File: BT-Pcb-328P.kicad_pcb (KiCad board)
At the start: 2 copper layers, 57 x 57 mm, 61 parts, among them J1 USB_B_Micro, J2 FTDI, J3 ICSP, J4 ANT, J5 Si7021, J6 Vin, P1 MYSX_2.6, Q1 FDN338P, Q2 FDN337N, Q3 FDN337N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

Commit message: Development 3
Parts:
- added C13: 100uF, Capacitor_SMD:CP_Elec_6.3x5.4, B.Cu at (168.9, 112.0)
- BT1, BT2: value Battery_Cell -> AAA Cell
- BT3: value Battery_Cell -> CR2032
- moved BT3 0.16 mm to (155.5, 126.2)
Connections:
- JP2 pad 1: Net-(C2-Pad1) -> Vraw
- JP2 pad 2: Vraw -> Net-(C2-Pad1)
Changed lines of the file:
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@@
     (tracks 0)
     (zones 0)
-    (modules 61)
+    (modules 62)
     (nets 59)
   )
@@
     (add_net Vraw)
   )
+  (module Capacitor_SMD:CP_Elec_6.3x5.4 (layer B.Cu)
+    (at 168.91 112.014 90)
+    (descr "SMD capacitor, aluminum electrolytic, Panasonic C55, 6.3x5.4mm")
+    (tags "capacitor electrolytic")
+    (attr smd)
+    (fp_text reference C13 (at 0 4.35 90) (layer B.SilkS)
+      (effects (font (size 1 1) (thickness 0.15)) (justify mirror))
+    )
+    (fp_text value 100uF (at 0 -4.35 90) (layer B.Fab)
+      (effects (font (size 1 1) (thickness 0.15)) (justify mirror))
+    )
+    (fp_circle (center 0 0) (end 3.15 0) (layer B.Fab) (width 0.1))
+    (fp_line (start 3.3 3.3) (end 3.3 -3.3) (layer B.Fab) (width 0.1))
+    (fp_line (start -2.3 3.3) (end 3.3 3.3) (layer B.Fab) (width 0.1))
+    (fp_line (start -2.3 -3.3) (end 3.3 -3.3) (layer B.Fab) (width 0.1))
+    (fp_line (start -3.3 2.3) (end -3.3 -2.3) (layer B.Fab) (width 0.1))
+    (fp_line (start -3.3 2.3) (end -2.3 3.3) (layer B.Fab) (width 0.1))
+    (fp_line (start -3.3 -2.3) (end -2.3 -3.3) (layer B.Fab) (width 0.1))
+    (fp_line (start -2.704838 1.33) (end -2.074838 1.33) (layer B.Fab) (width 0.1))
+    (fp_line (start -2.389838 1.645) (end -2.389838 1.015) (layer B.Fab) (width 0.1))
+    (fp_line (start 3.41 -3.41) (end 3.41 -1.06) (layer B.SilkS) (width 0.12))
+    (fp_line (start 3.41 3.41) (end 3.41 1.06) (layer B.SilkS) (width 0.12))
+    (fp_line (start -2.345563 3.41) (end 3.41 3.41) (layer B.SilkS) (width 0.12))
+    (fp_line (start -2.345563 -3.41) (end 3.41 -3.41) (layer B.SilkS) (width 0.12))
+    (fp_line (start -3.41 -2.345563) (end -3.41 -1.06) (layer B.SilkS) (width 0.12))
+    (fp_line (start -3.41 2.345563) (end -3.41 1.06) (layer B.SilkS) (width 0.12))
+    (fp_line (start -3.41 2.345563) (end -2.345563 3.41) (layer B.SilkS) (width 0.12))
+    (fp_line (start -3.41 -2.345563) (end -2.345563 -3.41) (layer B.SilkS) (width 0.12))
+    (fp_line (start -4.4375 1.8475) (end -3.65 1.8475) (layer B.SilkS) (width 0.12))
+    (fp_line (start -4.04375 2.24125) (end -4.04375 1.45375) (layer B.SilkS) (width 0.12))
+    (fp_line (start 3.55 3.55) (end 3.55 1.05) (layer B.CrtYd) (width 0.05))
+    (fp_line (start 3.55 1.05) (end 4.8 1.05) (layer B.CrtYd) (width 0.05))
+    (fp_line (start 4.8 1.05) (end 4.8 -1.05) (layer B.CrtYd) (width 0.05))
+    (fp_line (start 4.8 -1.05) (end 3.55 -1.05) (layer B.CrtYd) (width 0.05))
+    (fp_line (start 3.55 -1.05) (end 3.55 -3.55) (layer B.CrtYd) (width 0.05))
+    (fp_line (start -2.4 -3.55) (end 3.55 -3.55) (layer B.CrtYd) (width 0.05))
+    (fp_line (start -2.4 3.55) (end 3.55 3.55) (layer B.CrtYd) (width 0.05))
+    (fp_line (start -3.55 -2.4) (end -2.4 -3.55) (layer B.CrtYd) (width 0.05))
+    (fp_line (start -3.55 2.4) (end -2.4 3.55) (layer B.CrtYd) (width 0.05))
+    (fp_line (start -3.55 2.4) (end -3.55 1.05) (layer B.CrtYd) (width 0.05))
+    (fp_line (start -3.55 -1.05) (end -3.55 -2.4) (layer B.CrtYd) (width 0.05))
+    (fp_line (start -3.55 1.05) (end -4.8 1.05) (layer B.CrtYd) (width 0.05))
+    (fp_line (start -4.8 1.05) (end -4.8 -1.05) (layer B.CrtYd) (width 0.05))
+    (fp_line (start -4.8 -1.05) (end -3.55 -1.05) (layer B.CrtYd) (width 0.05))
+    (fp_text user %R (at 0 0 90) (layer B.Fab)
+      (effects (font (size 1 1) (thickness 0.15)) (justify mirror))
+    )
+    (pad 1 smd roundrect (at -2.8 0 90) (size 3.5 1.6) (layers B.Cu B.Paste B.Mask) (roundrect_rratio 0.15625)
+      (net 31 "Net-(BT1-Pad1)"))
+    (pad 2 smd roundrect (at 2.8 0 90) (size 3.5 1.6) (layers B.Cu B.Paste B.Mask) (roundrect_rratio 0.15625)
+      (net 9 GND))
+    (model ${KISYS3DMOD}/Capacitor_SMD.3dshapes/CP_Elec_6.3x5.4.wrl
+      (at (xyz 0 0 0))
+      (scale (xyz 1 1 1))
+      (rotate (xyz 0 0 0))
+    )
+  )
   (module batteries:AAA-Keystone-5204-5226-NO-SILK (layer B.Cu)
     (at 176.784 120.142 180)
@@
       (effects (font (size 1 1) (thickness 0.15)) (justify mirror))
     )
-    (fp_text value Battery_Cell (at 22 0 180) (layer B.Fab)
+    (fp_text value "AAA Cell" (at 22 0 180) (layer B.Fab)
       (effects (font (size 1 1) (thickness 0.15)) (justify mirror))
     )
@@
       (effects (font (size 1 1) (thickness 0.15)) (justify mirror))
     )
-    (fp_text value Battery_Cell (at 22 0) (layer B.Fab)
+    (fp_text value "AAA Cell" (at 22 0) (layer B.Fab)
       (effects (font (size 1 1) (thickness 0.15)) (justify mirror))
     )
@@
     )
   )
-  (module Battery:BatteryHolder_Keystone_1058_1x2032 (layer B.Cu)
-    (at 155.702 126.238 180)
+  (module Battery:BatteryHolder_Keystone_1058_1x2032 locked (layer B.Cu)
+    (at 155.54 126.238 180)
     (descr http://www.keyelco.com/product-pdf.cfm?p=14028)
     (tags "Keystone type 1058 coin cell retainer")
@@
       (effects (font (size 1 1) (thickness 0.15)) (justify mirror))
     )
-    (fp_text value Battery_Cell (at 0 9.398 180) (layer B.Fab)
+    (fp_text value CR2032 (at 0 9.398 180) (layer B.Fab)
       (effects (font (size 1 1) (thickness 0.15)) (justify mirror))
     )
@@
     (fp_line (start 1.65 1.25) (end -1.65 1.25) (layer F.CrtYd) (width 0.05))
     (pad 1 smd custom (at -0.65 0 180) (size 1 0.5) (layers F.Cu F.Mask)
-      (net 42 "Net-(C2-Pad1)") (zone_connect 0)
+      (net 23 Vraw) (zone_connect 0)
       (options (clearance outline) (anchor rect))
       (primitives
@@
       ))
     (pad 2 smd custom (at 0.65 0 180) (size 1 0.5) (layers F.Cu F.Mask)
-      (net 23 Vraw) (zone_connect 0)
+      (net 42 "Net-(C2-Pad1)") (zone_connect 0)
       (options (clearance outline) (anchor rect))
       (primitives

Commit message: Development 5
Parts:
- added C14: 47uF, Capacitor_SMD:CP_Elec_5x5.4, B.Cu at (172.7, 101.1)
- added U7: NRF24L01, mysensors_radios:NRF24L01, B.Cu at (179.1, 81.8)
- added U8: NRF24L01, mysensors_radios:NRF24L01-SMD, B.Cu at (149.9, 94.2)
- moved C13 2.09 mm to (168.4, 110.0), turned to 0 degrees
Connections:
- J5 pad 2: VCC -> D8
- JP3 pad 1: D8 -> D9
- R10 pad 2: D9 -> D5
- R6 pad 1: D5 -> D8
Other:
- net class Default: trace_width 0.25 -> 0.16; via_dia 0.8 -> 0.65; via_drill 0.4 -> 0.35
- rule trace_min: 0.2 -> 0.16
- rule via_min_drill: 0.3 -> 0.35
- rule via_min_size: 0.4 -> 0.65

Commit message: Development 6
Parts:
- added REF**: MountingHole_1.5mm, holes:MountingHole_1.5mm, F.Cu at (146.8, 120.7)
- added REF**: MountingHole_1.5mm, holes:MountingHole_1.5mm, F.Cu at (144.6, 118.6)
- added REF**: MountingHole_1.5mm, holes:MountingHole_1.5mm, F.Cu at (144.6, 101.1)
- added REF**: MountingHole_1.5mm, holes:MountingHole_1.5mm, F.Cu at (146.8, 98.9)
- added REF**: MountingHole_1.5mm, holes:MountingHole_1.5mm, F.Cu at (164.3, 120.7)
- added REF**: MountingHole_1.5mm, holes:MountingHole_1.5mm, F.Cu at (166.4, 118.6)
- added REF**: MountingHole_1.5mm, holes:MountingHole_1.5mm, F.Cu at (166.4, 101.1)
- added REF**: MountingHole_1.5mm, holes:MountingHole_1.5mm, F.Cu at (164.3, 98.9)
- moved C1 10.3 mm to (169.8, 119.7), turned to 270 degrees
- moved J6 10.2 mm to (182.0, 135.1), turned to 180 degrees
- moved J1 8.13 mm to (181.4, 125.7)
- moved C2 5.67 mm to (173.6, 131.2)
- moved R1 4.57 mm to (170.1, 115.1)
- moved D1 3.09 mm to (169.9, 107.6)
- moved U1 1.27 mm to (173.2, 126.2)
- moved JP2 0.40 mm to (176.9, 136.3), turned to 0 degrees
- moved Q1 0.38 mm to (173.7, 119.3)
- moved C12 0.25 mm to (128.5, 92.3)
- moved C4 0.25 mm to (128.5, 95.8)
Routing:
- net VCC: track 0.00 -> 279.6 mm, vias 0 -> 20
- net GND: track 0.00 -> 192.7 mm, vias 0 -> 27
- net RESET: track 0.00 -> 151.5 mm, vias 0 -> 8
- net A3: track 0.00 -> 137.2 mm, vias 0 -> 7
- net Net-(C1-Pad1): track 0.00 -> 115.4 mm, vias 0 -> 7
- net Vraw: track 0.00 -> 102.3 mm, vias 0 -> 1
- net +3.3V: track 0.00 -> 98.9 mm, vias 0 -> 5
- net D3: track 0.00 -> 93.9 mm, vias 0 -> 8
- net D2: track 0.00 -> 92.4 mm, vias 0 -> 4
- net MOSI: track 0.00 -> 86.3 mm, vias 0 -> 6
- net D9: track 0.00 -> 85.1 mm, vias 0 -> 5
- net MISO: track 0.00 -> 83.9 mm, vias 0 -> 2
- net A2: track 0.00 -> 80.9 mm, vias 0 -> 7
- net SCK: track 0.00 -> 75.8 mm, vias 0 -> 1
- net D4: track 0.00 -> 75.3 mm, vias 0 -> 5
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- added copper zone on B.Cu, net GND
- added copper zone on F.Cu, net GND
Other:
- outline, holes or cut-outs redrawn

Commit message: BP-Pcb-328P v.1.0
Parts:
- added G***: LOGO, logo:d-diot-logo-small, B.Cu at (155.4, 125.3)
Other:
- rule pad_to_mask_clearance: 0.051 -> 0.049
- rule solder_mask_min_width: 0.25 -> 0.1
- board text added: "ANT"
- board text added: "BT-PCB-328P v.1.0"
- board text added: "FTDI"
- board text added: "ICSP"
- board text added: "Si7021"

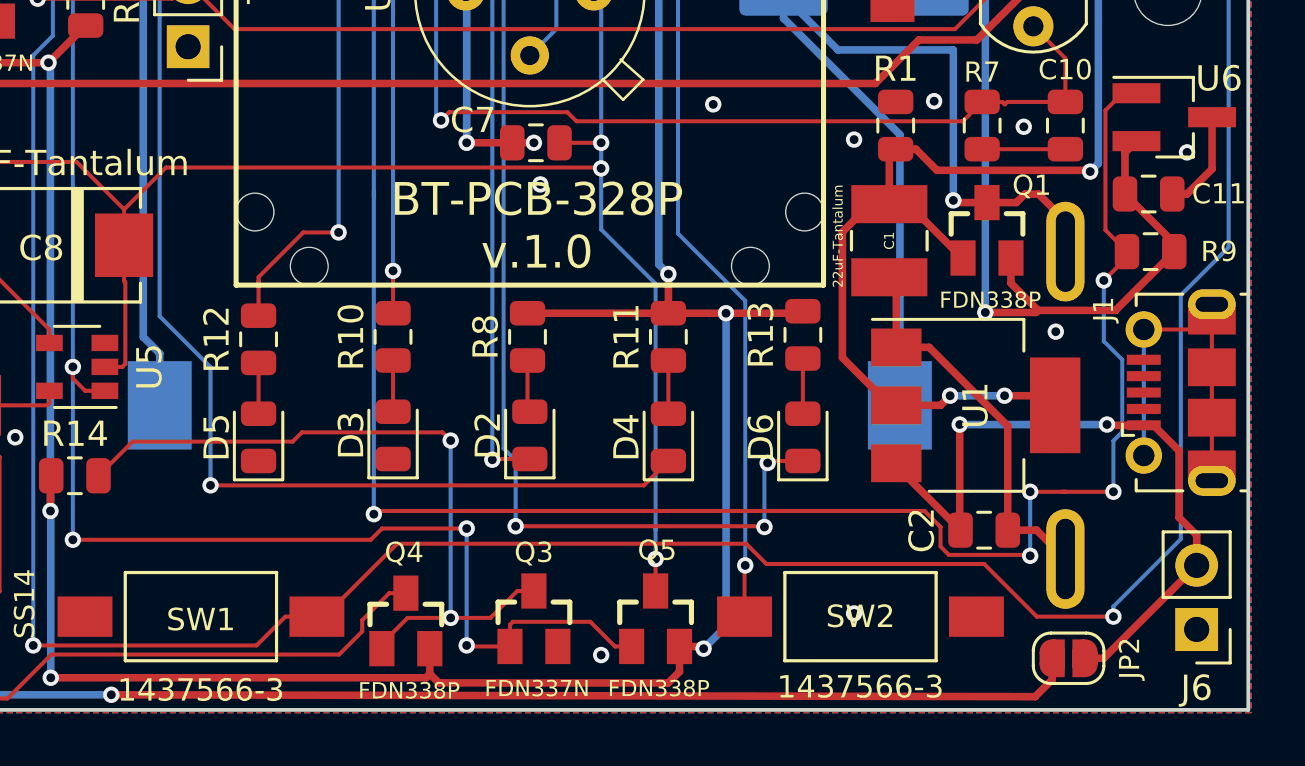
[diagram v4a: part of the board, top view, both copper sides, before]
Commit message: Added Vin + and - text
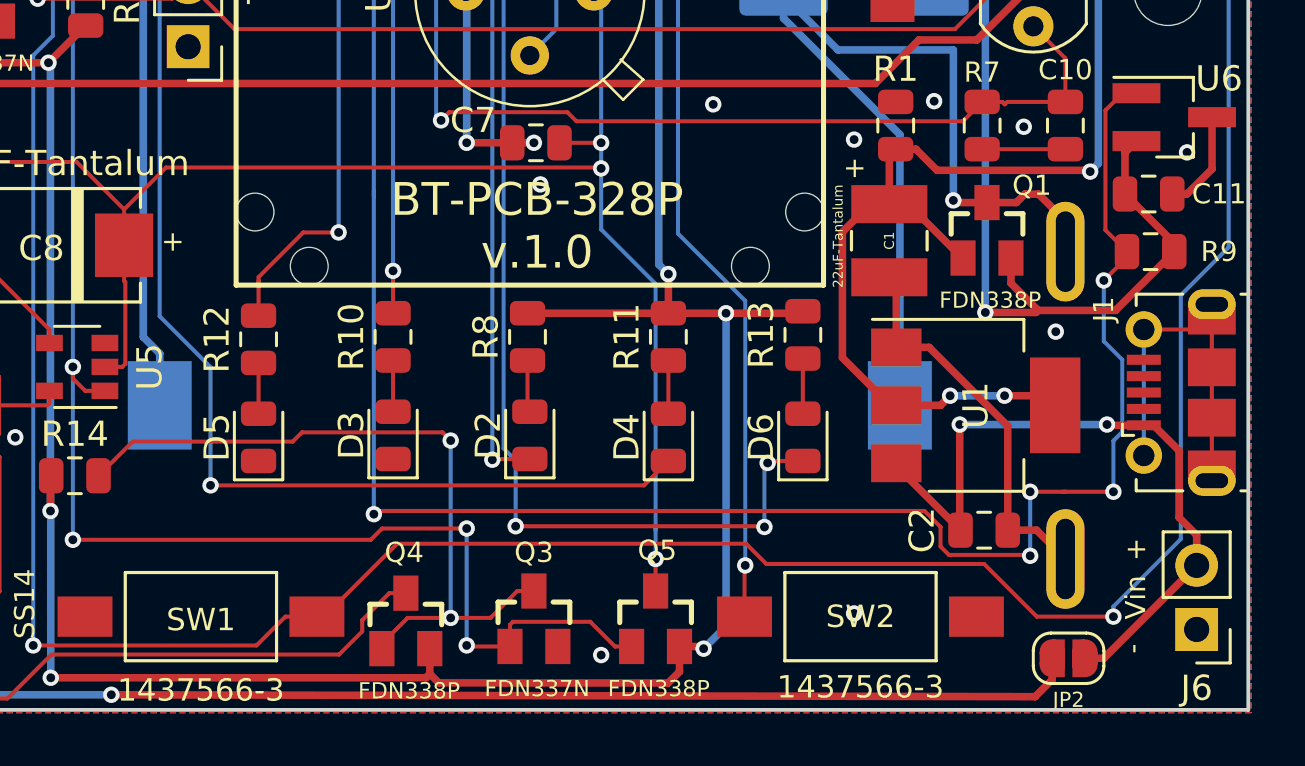
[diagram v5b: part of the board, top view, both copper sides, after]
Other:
- board text added: "+"
- board text added: "-"
- board text added: "Vin"
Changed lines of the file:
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@@
   (general
     (thickness 1.6)
-    (drawings 13)
+    (drawings 18)
     (tracks 962)
     (zones 0)
@@
     (tags "solder jumper open")
     (attr virtual)
-    (fp_text reference JP2 (at 2.428 0 90) (layer F.SilkS)
-      (effects (font (size 0.8 0.8) (thickness 0.12)))
+    (fp_text reference JP2 (at 0 1.651 180) (layer F.SilkS)
+      (effects (font (size 0.6 0.6) (thickness 0.1)))
     )
     (fp_text value Vraw (at 0 1.9) (layer F.Fab)
@@
       (xy -0.339993 -3.369811) (xy -0.309687 -3.369775) (xy -0.275638 -3.369787)) (layer B.SilkS) (width 0.01))
   )
+  (gr_text "+\n" (at 141.351 119.761 90) (layer F.SilkS)
+    (effects (font (size 0.8 0.8) (thickness 0.12)))
+  )
+  (gr_text "+\n" (at 168.402 116.84 90) (layer F.SilkS)
+    (effects (font (size 0.8 0.8) (thickness 0.12)))
+  )
+  (gr_text "+\n" (at 179.578 131.953 90) (layer F.SilkS)
+    (effects (font (size 0.8 0.8) (thickness 0.12)))
+  )
+  (gr_text - (at 179.451 135.89 90) (layer F.SilkS)
+    (effects (font (size 0.8 0.8) (thickness 0.12)))
+  )
+  (gr_text Vin (at 179.578 133.858 90) (layer F.SilkS)
+    (effects (font (size 0.8 0.8) (thickness 0.12)))
+  )
   (gr_text "BT-PCB-328P\nv.1.0" (at 155.829 119.126) (layer F.SilkS)

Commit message: board v.2.0
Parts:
- removed D7: SS14, diodes:SS14
- removed Q4, Q5: FDN338P, FDN338P:SSOT-3
- removed R14: 1M, Resistor_SMD:R_0805_2012Metric
- R10: value 330 -> 120
- U2: footprint as312:as312 -> as312:PIR-AS312-3PIN
- moved JP2 45.1 mm to (131.8, 136.1)
- moved G*** 35.1 mm to (140.2, 93.7)
- moved R10 12.8 mm to (160.5, 130.9)
- moved D3 12.7 mm to (160.5, 134.7)
- moved D2 10.9 mm to (144.8, 129.3)
- moved R8 10.7 mm to (144.8, 123.5)
- moved R12 9.46 mm to (150.6, 131.1)
- moved D5 9.26 mm to (150.6, 134.7)
- moved C9 5.93 mm to (133.3, 132.2)
- moved D4 5.78 mm to (155.5, 129.3)
- moved R11 5.50 mm to (155.5, 123.5)
- moved D6 1.78 mm to (166.4, 129.3)
- moved BT3 1.60 mm to (155.5, 127.8)
- moved Q3 0.88 mm to (155.4, 133.9)
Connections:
- C9 pad 2: Net-(C9-Pad2) -> VCC
- D3 pad 1: GND -> Net-(D3-Pad1)
- L1 pad 1: Net-(C9-Pad2) -> VCC
- Q3 pad 1: D4 -> D5
- Q3 pad 3: Net-(Q3-Pad3) -> Net-(D3-Pad1)
- R10 pad 2: D5 -> +3.3V
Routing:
- net Vraw: track 102.3 -> 54.3 mm
- net Net-(C2-Pad1): track 28.3 -> 74.7 mm
- net Net-(C9-Pad2): track 37.6 -> 0.00 mm
- net D4: track 75.3 -> 41.9 mm, vias 5 -> 2
- net Net-(Q3-Pad3): track 28.9 -> 0.00 mm, vias 2 -> 0
- net VCC: track 279.6 -> 298.6 mm
- net D5: track 61.6 -> 76.0 mm, vias 4 -> 5
- net Net-(L1-Pad2): track 14.0 -> 2.91 mm
- net Net-(D3-Pad1): track 0.00 -> 8.71 mm
- net D6: track 64.1 -> 72.7 mm, vias 5 -> 4
- net Net-(R4-Pad2): track 13.2 -> 6.58 mm
- net GND: track 192.7 -> 198.5 mm
- net RESET: track 151.5 -> 157.0 mm, vias 8 -> 10
- net A2: track 80.9 -> 75.5 mm, vias 7 -> 5
- net A5-SCL: track 34.0 -> 29.8 mm
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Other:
- board text added: "BT-PCB-328P v.2.0"
- board text removed: "BT-PCB-328P v.1.0"

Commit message: board v.3.0
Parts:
- removed U8: NRF24L01, mysensors_radios:NRF24L01-SMD
- moved D4 25.5 mm to (162.1, 104.6), turned to 0 degrees
- moved R5 24.6 mm to (144.5, 123.7)
- moved D6 19.5 mm to (162.1, 110.2), turned to 0 degrees
- moved D2 19.5 mm to (148.8, 110.2), turned to 180 degrees
- moved D3 18.9 mm to (162.1, 115.8), turned to 0 degrees
- moved D5 18.9 mm to (149.1, 115.8), turned to 180 degrees
- moved Q3 10.2 mm to (155.2, 123.7), turned to 270 degrees
- moved R11 9.56 mm to (165.1, 123.8), turned to 270 degrees
- moved R10 7.47 mm to (158.5, 123.7), turned to 270 degrees
- moved R12 7.38 mm to (151.1, 123.7), turned to 270 degrees
- moved R13 4.58 mm to (161.8, 123.8), turned to 270 degrees
- moved R8 3.06 mm to (147.8, 123.8), turned to 270 degrees
- moved R4 1.85 mm to (150.4, 106.2)
- moved Q2 0.65 mm to (154.9, 103.1), turned to 90 degrees
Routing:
- net GND: track 198.5 -> 233.6 mm, vias 27 -> 26
- net A2: track 75.5 -> 47.9 mm
- net A0: track 59.7 -> 36.0 mm
- net A1: track 69.4 -> 48.2 mm, vias 4 -> 6
- net Net-(D6-Pad2): track 3.97 -> 19.8 mm, vias 0 -> 4
- net Net-(D4-Pad2): track 3.89 -> 19.7 mm, vias 0 -> 2
- net D5: track 76.0 -> 62.8 mm, vias 5 -> 2
- net Net-(D3-Pad2): track 1.94 -> 13.8 mm
- net Net-(D2-Pad2): track 4.00 -> 14.3 mm, vias 0 -> 2
- net Net-(D5-Pad2): track 1.76 -> 11.8 mm, vias 0 -> 2
- net SCK: track 75.8 -> 66.7 mm
- net D3: track 97.5 -> 106.1 mm, vias 8 -> 7
- net VCC: track 298.6 -> 291.0 mm, vias 20 -> 19
- net NSS: track 71.8 -> 69.5 mm
- net D2: track 92.4 -> 94.5 mm
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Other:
- board text added: "BT-PCB-328P v.3.0"
- board text removed: "BT-PCB-328P v.2.0"

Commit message: readded nrf24l01 smd footprint
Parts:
- added U8: NRF24L01, mysensors_radios:NRF24L01-SMD, B.Cu at (149.9, 94.2)
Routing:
- net SCK: track 66.7 -> 76.2 mm, vias 1 -> 2
- net VCC: track 291.0 -> 296.2 mm
- net D2: track 94.5 -> 98.0 mm
- net NSS: track 69.5 -> 71.8 mm
- net D9: track 83.1 -> 85.2 mm
